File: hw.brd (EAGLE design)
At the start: 80 x 80 mm, 48 parts, among them IC1 MIC_I2S_SPH0645, IC2 CP2104, Q1 mmbt2222, Q2 mmbt2222, Q3 DMG3415U, SW2 KMR2, U1 MAX98357A, U2 AP2112-3.3, U3 MCP73831T-2ACI/OT, X2 JSTPH, X3 ESP32_WROOM32_SKINNY, X4 20329

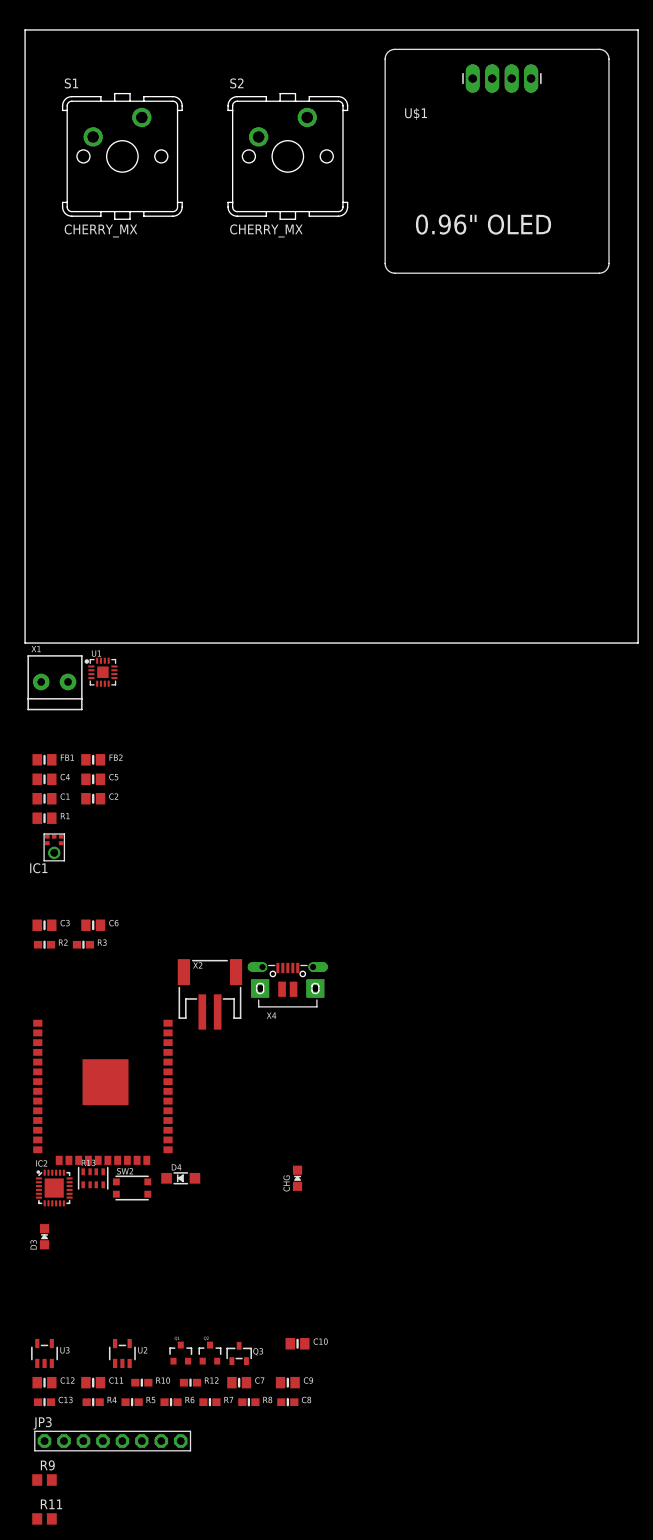
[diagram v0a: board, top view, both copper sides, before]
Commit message: using assembled esp32 devkitv1
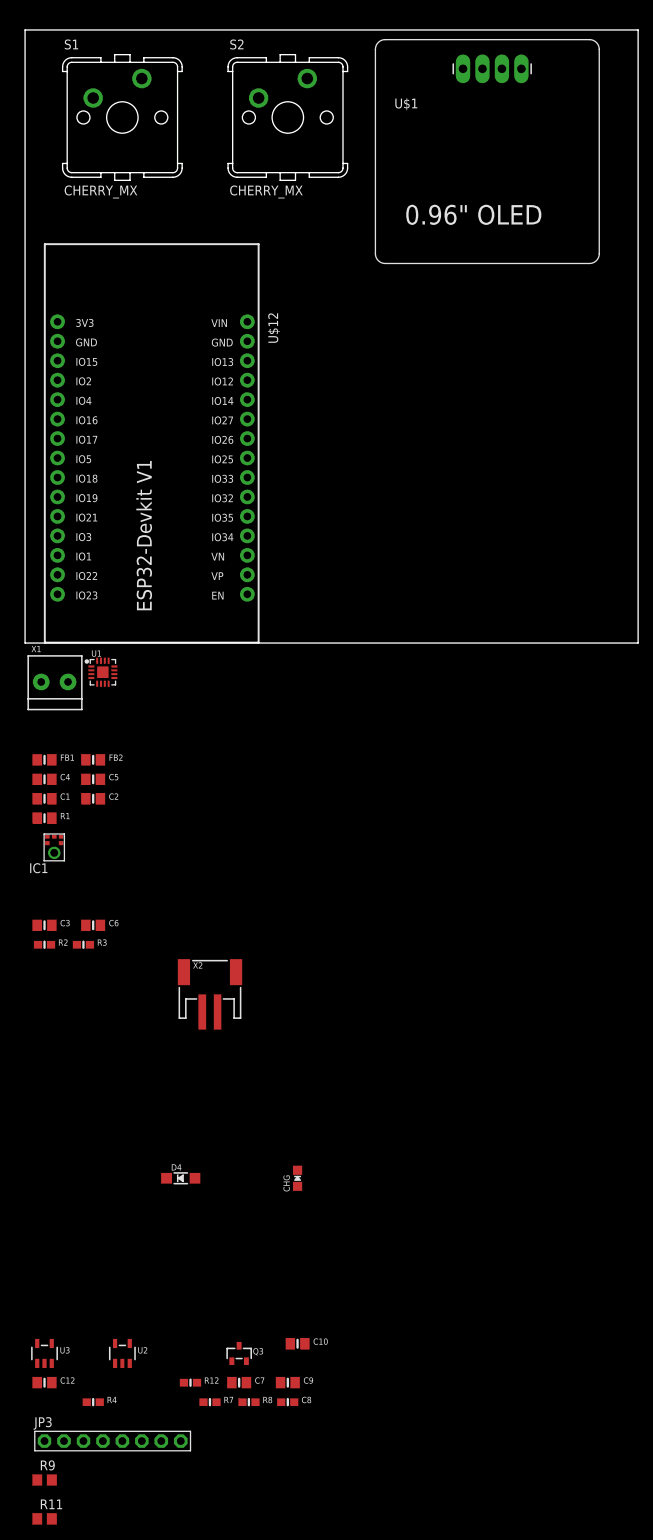
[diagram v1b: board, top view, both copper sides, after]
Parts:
- removed C11: 10uF, microbuilder:0805-NO
- removed C13: 1uF, microbuilder:0603-NO
- removed D3: RED, microbuilder:CHIPLED_0805_NOOUTLINE
- removed IC2: CP2104, microbuilder:QFN24_4MM_SMSC
- removed Q1, Q2: mmbt2222, SparkFun:SOT23-3
- removed R10: 1K, microbuilder:0603-NO
- removed R13: 10K, microbuilder:RESPACK_4X0603
- removed R5, R6: 100K, microbuilder:0603-NO
- removed SW2: KMR2, microbuilder:BTN_KMR2_4.6X2.8
- removed X3: ESP32_WROOM32_SKINNY, microbuilder:WROOM32_SKINNY
- removed X4: 20329, microbuilder:4UCONN_20329_V2
- added U$12: ESP32DEVKITV1, ESP32-DEVKITV1:ESP32-DEVKITV1
- moved S1 5.08 mm to (12.7, 68.6)
- moved S2 5.08 mm to (34.3, 68.6)
- moved U$1 1.80 mm to (57.1, 74.9)
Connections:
- removed net A0_DAC2: X3.11
- removed net A13_I35: R5.1, R6.2, X3.7
- removed net A1_DAC1: X3.10
- removed net A2_I34: X3.6
- removed net A3_I39: X3.5
- removed net A4_IO36: X3.4
- removed net A5_IO4: X3.26
- removed net DTR: IC2.23, Q2.2, R13.4
- removed net GPIO0: Q2.3, X3.25
- removed net GPIO2: X3.24
- removed net IO12_A11: X3.14
- removed net IO13_A12: R10.1, X3.16
- removed net IO14_A6: X3.13
- removed net IO15_A8: X3.23
- removed net IO16: X3.27
- removed net IO17: X3.28
- removed net IO21: X3.33
- removed net IO27_A10: X3.12
- removed net IO32_A7: X3.8
- removed net IO33_A9: X3.9
- removed net MISO: X3.31
- removed net MOSI: X3.30
- removed net N$10: D3.A, R10.2
- removed net N$12: Q1.1, R13.5
- removed net N$13: Q2.1, R13.2
- removed net N$7: IC2.3, X4.D+
- removed net N$8: IC2.4, X4.D-
- removed net RESET: C13.1, Q1.3, R13.6, SW2.B, SW2.B', X3.3
- removed net RTS: IC2.19, Q1.2, R13.7
- removed net RXD0: IC2.21, X3.34
- removed net SCK: X3.29
- removed net TXD0: IC2.20, X3.35
- net 3.3V: no longer C11.1, IC2.5, IC2.6, IC2.7, R13.3, X3.2
- net GND: no longer C11.2, C13.2, D3.C, IC2.2, IC2.THERM, R6.1, SW2.A, SW2.A', X3.1, X3.15, X3.38, X3.P$1, X4.BASE@1, X4.BASE@2, X4.GND, X4.SPRT@1, X4.SPRT@2, X4.SPRT@3, X4.SPRT@4
- net SCL: no longer X3.36
- net SDA: no longer X3.37
- net VBAT: no longer R5.2
- net VBUS: no longer IC2.8, X4.VBUS

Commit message: routing
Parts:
- removed JP3: (no value), adafruit:1X08-BIG
- added JP1: (no value), microbuilder:1X07_ROUND_76
- added JP2: (no value), microbuilder:1X06_ROUND
- R11, R9: value (none) -> 10k
- moved R11 113.6 mm to (22.9, -2.54), flipped to the bottom, turned to 180 degrees
- moved R9 103.6 mm to (22.9, -7.62), flipped to the bottom, turned to 180 degrees
- moved C3 100.2 mm to (40.6, 55.9), flipped to the bottom
- moved R2 96.6 mm to (45.7, 47.0), flipped to the bottom, turned to 180 degrees
- moved R3 96.0 mm to (40.6, 50.8), flipped to the bottom, turned to 180 degrees
- moved C6 95.6 mm to (40.6, 53.3), flipped to the bottom
- moved C8 83.8 mm to (54.6, -17.8), flipped to the bottom, turned to 180 degrees
- moved R4 83.8 mm to (29.2, -17.8), flipped to the bottom, turned to 180 degrees
- moved R7 83.8 mm to (44.5, -17.8), flipped to the bottom, turned to 180 degrees
- moved R8 83.8 mm to (49.5, -17.8), flipped to the bottom, turned to 180 degrees
- moved IC1 81.8 mm to (39.4, 47.0), flipped to the bottom, turned to 90 degrees
- moved C12 78.9 mm to (22.9, -20.3), flipped to the bottom, turned to 180 degrees
- moved C7 78.9 mm to (48.3, -20.3), flipped to the bottom, turned to 180 degrees
- moved C9 78.9 mm to (54.6, -20.3), flipped to the bottom, turned to 180 degrees
- moved R12 78.9 mm to (41.9, -20.3), flipped to the bottom, turned to 180 degrees
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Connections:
- new net BTN1: S2.S2, U$12.15
- new net BTN2: S1.S2, U$12.14
- new net DATA: JP2.4, U$12.24
- new net N$12: U$12.24
- net BCLK: now also JP1.6, JP2.3, U$12.21; no longer JP3.1
- net DIN: now also JP1.5, U$12.23; no longer JP3.3
- net DOUT: no longer JP3.4
- net GAIN: now also JP1.4
- net GND: now also JP1.2, JP2.2, S1.S1, S2.S1; no longer JP3.8
- net LRCLK: now also JP1.7, JP2.5, U$12.22; no longer JP3.2
- net SD_MODE: now also JP1.3; no longer JP3.6
- net SELECT: now also JP2.6, U$12.26; no longer JP3.5
- net VDD: now also JP1.1, JP2.1; no longer JP3.7
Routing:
- net GND: track 0.00 -> 144.0 mm
- net BCLK: track 0.00 -> 33.6 mm
- net LRCLK: track 0.00 -> 32.6 mm
- net VDD: track 0.00 -> 30.5 mm

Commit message: more routing
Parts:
- moved R9 87.5 mm to (63.5, 69.8), turned to 270 degrees
- moved R11 81.8 mm to (61.0, 69.8), turned to 270 degrees
- moved U2 60.2 mm to (40.6, 35.6), turned to 90 degrees
- moved C7 57.6 mm to (34.3, 35.6), turned to 90 degrees
- moved C12 57.1 mm to (43.2, 33.0)
- moved R7 53.9 mm to (36.8, 35.6), turned to 270 degrees
- moved C9 52.1 mm to (43.2, 30.5)
- moved U3 47.2 mm to (41.9, 19.1), turned to 0 degrees
- moved C8 47.1 mm to (43.2, 27.9)
- moved Q3 44.7 mm to (36.8, 19.1)
- moved R12 44.5 mm to (41.9, 24.1), turned to 270 degrees
- moved C10 42.2 mm to (40.6, 14.0), turned to 270 degrees
- moved R8 42.2 mm to (44.5, 24.1), turned to 270 degrees
- moved R4 37.0 mm to (33.0, 19.1), turned to 270 degrees
- moved D4 33.3 mm to (36.8, 24.1)
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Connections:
- removed net DATA: JP2.4, U$12.24
- net DOUT: now also JP2.4, U$12.24
- net SCL: now also U$12.10
- net SDA: now also U$12.11
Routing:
- net GND: track 144.0 -> 215.8 mm
- net VBAT: track 0.00 -> 27.6 mm
- net DOUT: track 0.00 -> 25.6 mm
- net N$9: track 0.00 -> 20.3 mm
- net VO-: track 0.00 -> 18.0 mm
- net VDD: track 30.5 -> 14.7 mm
- net N$3: track 0.00 -> 11.3 mm
- net VCC: track 0.00 -> 10.9 mm
- net VBUS: track 0.00 -> 9.83 mm
- net N$5: track 0.00 -> 9.00 mm
- net VO+: track 0.00 -> 8.74 mm
- net 3.3V: track 0.00 -> 6.83 mm
- net LRCLK: track 32.6 -> 38.4 mm
- net SDA: track 0.00 -> 5.40 mm
- net SCL: track 0.00 -> 5.40 mm
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
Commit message: rerouting :|
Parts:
- moved X1 52.3 mm to (33.0, 52.1), turned to 270 degrees
- moved FB1 43.9 mm to (26.7, 53.3), turned to 180 degrees
- moved FB2 43.2 mm to (26.7, 50.8), turned to 180 degrees
- moved C2 41.9 mm to (20.3, 55.9), turned to 0 degrees
- moved C4 41.4 mm to (26.7, 48.3), turned to 0 degrees
- moved C1 39.5 mm to (20.3, 53.3), turned to 0 degrees
- moved C5 36.6 mm to (26.7, 45.7), turned to 0 degrees
- moved C3 34.2 mm to (15.2, 33.0), turned to 0 degrees
- moved C6 34.2 mm to (15.2, 30.5), turned to 0 degrees
- moved R4 33.0 mm to (66.0, 20.3), turned to 0 degrees
- moved R1 33.0 mm to (20.3, 50.8)
- moved CHG 33.0 mm to (66.0, 22.9), turned to 90 degrees
- moved U1 29.6 mm to (20.3, 47.0), turned to 180 degrees
- moved R3 25.4 mm to (20.3, 35.6)
- moved IC1 23.6 mm to (20.3, 33.0)
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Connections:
- removed net N$12: U$12.24
- removed net VCC: R11.2, R9.2, U$1.4
- removed net WS: IC1.1
- net 3.3V: now also C1.1, C2.1, C3.1, C6.1, IC1.5, JP1.1, JP2.1, R1.2, U$12.1, U1.7, U1.8
- net BCLK: now also U$12.7; no longer U$12.21
- net BTN1: now also U$12.27; no longer U$12.15
- net BTN2: now also U$12.28; no longer U$12.14
- net DIN: now also U$12.9; no longer U$12.23
- net DOUT: now also U$12.5; no longer U$12.24
- net GAIN: no longer JP1.4
- net GND: now also U$12.2
- net LRCLK: now also IC1.1, U$12.6; no longer U$12.22
- net SCL: now also U$12.11; no longer U$12.10
- net SDA: now also U$12.10; no longer U$12.11
- net SD_MODE: no longer JP1.3
- net SELECT: no longer JP2.6, U$12.26
- net VDD: now also R11.2, R9.2, U$1.4, U$12.30; no longer C1.1, C2.1, C3.1, C6.1, IC1.5, JP1.1, JP2.1, R1.2, U1.7, U1.8
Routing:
- net GND: track 215.8 -> 0.00 mm
- net SCL: track 5.40 -> 142.6 mm
- net SDA: track 5.40 -> 136.4 mm
- net 3.3V: track 6.83 -> 116.5 mm
- net DIN: track 0.00 -> 104.8 mm
- net LRCLK: track 38.4 -> 141.7 mm
- net BTN2: track 0.00 -> 86.5 mm
- net BCLK: track 33.6 -> 113.6 mm
- net BTN1: track 0.00 -> 65.7 mm
- net VDD: track 14.7 -> 48.8 mm
- net DOUT: track 25.6 -> 50.3 mm
- net VBAT: track 27.6 -> 14.3 mm
- net VO+: track 8.74 -> 20.9 mm
- net VCC: track 10.9 -> 0.00 mm
- net N$3: track 11.3 -> 2.52 mm
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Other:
- board size 80 x 80 mm -> 81.3 x 81.3 mm

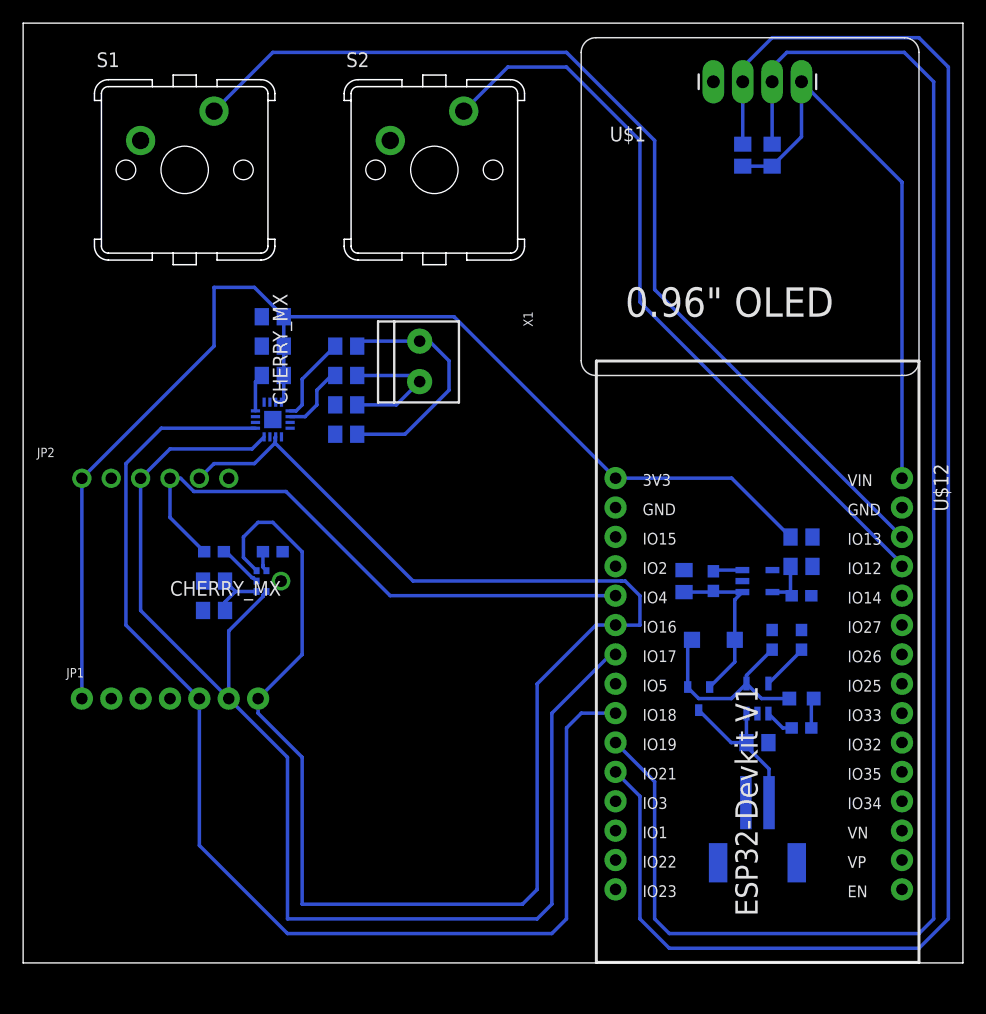
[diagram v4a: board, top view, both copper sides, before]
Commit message: it works out!
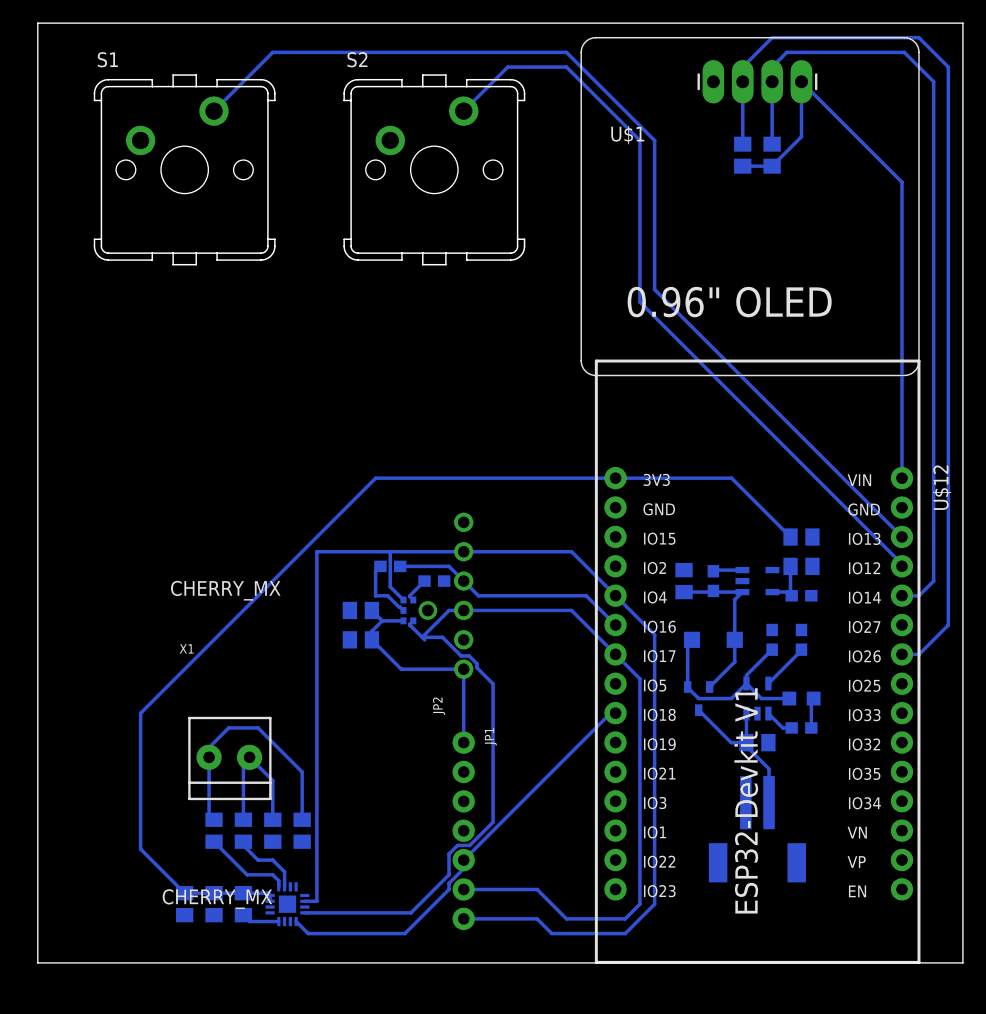
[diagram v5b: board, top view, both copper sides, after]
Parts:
- moved C2 51.4 mm to (12.7, 5.08), turned to 270 degrees
- moved C1 48.5 mm to (15.2, 5.08), turned to 270 degrees
- moved R1 45.8 mm to (17.8, 5.08), turned to 90 degrees
- moved FB1 43.4 mm to (15.2, 11.4), turned to 90 degrees
- moved U1 41.9 mm to (21.6, 5.08), turned to 90 degrees
- moved FB2 40.4 mm to (17.8, 11.4), turned to 90 degrees
- moved X1 38.1 mm to (16.5, 17.8), turned to 0 degrees
- moved C4 37.4 mm to (20.3, 11.4), turned to 270 degrees
- moved C5 34.5 mm to (22.9, 11.4), turned to 270 degrees
- moved JP2 28.5 mm to (36.8, 31.8), turned to 90 degrees
- moved JP1 27.9 mm to (36.8, 11.4), turned to 270 degrees
- moved R2 15.3 mm to (30.5, 34.3), turned to 180 degrees
- moved R3 14.2 mm to (34.3, 33.0)
- moved IC1 13.0 mm to (33.0, 30.5)
- moved C3 13.0 mm to (27.9, 30.5)
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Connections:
- net DOUT: now also U$12.6; no longer U$12.5
- net LRCLK: now also U$12.5; no longer U$12.6
- net SCL: now also U$12.24; no longer U$12.11
- net SDA: now also U$12.26; no longer U$12.10
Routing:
- net DIN: track 104.8 -> 36.7 mm
- net SDA: track 136.4 -> 68.7 mm
- net SCL: track 142.6 -> 79.9 mm
- net LRCLK: track 141.7 -> 109.5 mm
- net DOUT: track 50.3 -> 20.7 mm
- net BCLK: track 113.6 -> 101.8 mm
- net N$1: track 3.88 -> 5.65 mm
- net SELECT: track 1.76 -> 2.28 mm
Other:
- board size 81.3 x 81.3 mm -> 80 x 81.3 mm
